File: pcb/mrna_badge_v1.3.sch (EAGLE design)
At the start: 45 parts, among them T1 FS8205, U3 ATTINY24A-MUFOOT

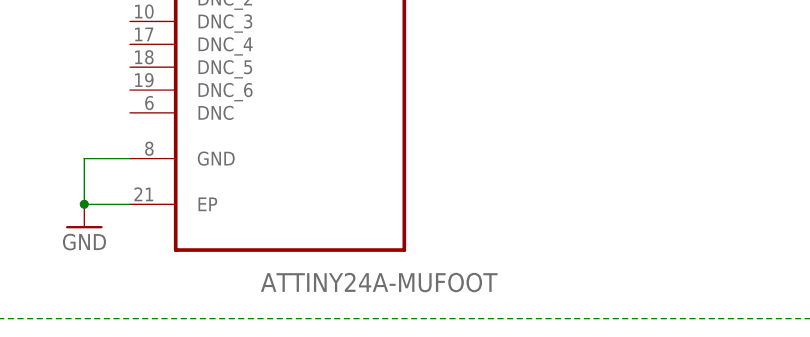
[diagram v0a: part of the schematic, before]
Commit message: patches from v1.2 fixed for v1.3
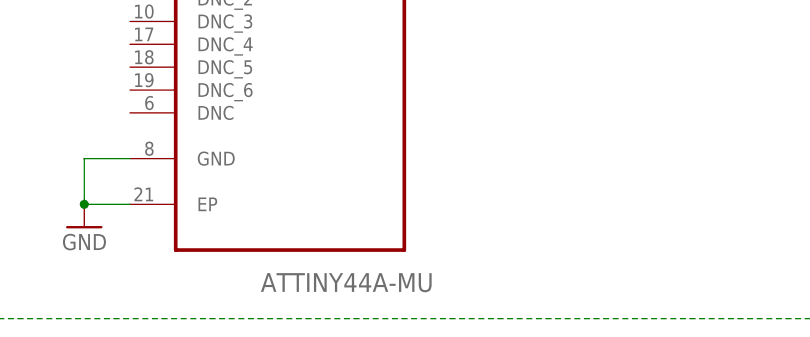
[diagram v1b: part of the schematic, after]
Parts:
- U3: value ATTINY24A-MUFOOT -> ATTINY44A-MU
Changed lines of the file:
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@@
 <part name="+3V8" library="supply1" deviceset="+3V3" device=""/>
 <part name="+3V9" library="supply1" deviceset="+3V3" device=""/>
-<part name="U3" library="Atmel_By_element14_Batch_1-00" deviceset="ATTINY24A-MU" device="FOOT" value="ATTINY24A-MUFOOT"/>
+<part name="U3" library="Atmel_By_element14_Batch_1-00" deviceset="ATTINY24A-MU" device="FOOT" value="ATTINY44A-MU"/>
 <part name="GND7" library="supply1" deviceset="GND" device=""/>
 <part name="3V1" library="supply1" deviceset="+3V3" device=""/>
